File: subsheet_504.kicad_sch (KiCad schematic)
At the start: 36 parts, among them J502 Phono LEFT, J503 Phono RIGHT, U504 LF347N_mu, U508 LMC1992CCN_PHY

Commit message: pcb session 2023-01-21T22:41:51+01:00
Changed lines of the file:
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@@
     (pin "9")
   )
-  (symbol (lib_id "Device:CP1") (at 88.9 59.69 0)
+  (symbol (lib_id "Device:CP1") (at 88.9 59.69 0) (unit 1)
     (in_bom yes) (on_board yes)
     (property "Reference" "CP535" (id 0) (at 90.17 57.15 0)
@@
     (pin "2")
   )
-  (symbol (lib_id "Device:R_Small_US") (at 76.2 59.69 0)
+  (symbol (lib_id "Device:R_Small_US") (at 76.2 59.69 0) (unit 1)
     (in_bom yes) (on_board yes)
     (property "Reference" "R530" (id 0) (at 77.47 58.42 0)
@@
     (pin "2")
   )
-  (symbol (lib_id "Device:C_Small") (at 101.6 59.69 0)
+  (symbol (lib_id "Device:C_Small") (at 101.6 59.69 0) (unit 1)
     (in_bom yes) (on_board yes)
     (property "Reference" "C536" (id 0) (at 102.87 57.15 0)
@@
     (pin "2")
   )
-  (symbol (lib_id "Device:CP1") (at 38.1 26.67 270)
+  (symbol (lib_id "Device:CP1") (at 38.1 26.67 270) (unit 1)
     (in_bom yes) (on_board yes)
     (property "Reference" "CP541" (id 0) (at 35.56 22.86 90)
@@
     (pin "2")
   )
-  (symbol (lib_id "Device:CP1") (at 38.1 39.37 270)
+  (symbol (lib_id "Device:CP1") (at 38.1 39.37 270) (unit 1)
     (in_bom yes) (on_board yes)
     (property "Reference" "CP546" (id 0) (at 35.56 35.56 90)
@@
     (pin "2")
   )
-  (symbol (lib_id "Device:CP1") (at 35.56 96.52 270)
+  (symbol (lib_id "Device:CP1") (at 35.56 96.52 270) (unit 1)
     (in_bom yes) (on_board yes)
     (property "Reference" "CP544" (id 0) (at 26.67 95.25 90)
@@
     (pin "2")
   )
-  (symbol (lib_id "Device:CP1") (at 172.72 93.98 90)
+  (symbol (lib_id "Device:CP1") (at 172.72 93.98 90) (unit 1)
     (in_bom yes) (on_board yes)
     (property "Reference" "CP547" (id 0) (at 170.18 92.71 90)
@@
     (pin "2")
   )
-  (symbol (lib_id "Device:R_Small_US") (at 88.9 25.4 0)
+  (symbol (lib_id "Device:R_Small_US") (at 88.9 25.4 0) (unit 1)
     (in_bom yes) (on_board yes)
     (property "Reference" "R525" (id 0) (at 90.17 24.13 0)
@@
     (pin "2")
   )
-  (symbol (lib_id "Device:R_Small_US") (at 78.74 33.02 90)
+  (symbol (lib_id "Device:R_Small_US") (at 78.74 33.02 90) (unit 1)
     (in_bom yes) (on_board yes)
     (property "Reference" "R531" (id 0) (at 81.28 30.48 90)
@@
     (pin "2")
   )
-  (symbol (lib_id "Device:R_Small_US") (at 97.79 41.91 180)
+  (symbol (lib_id "Device:R_Small_US") (at 97.79 41.91 180) (unit 1)
     (in_bom yes) (on_board yes)
     (property "Reference" "R539" (id 0) (at 104.14 40.64 0)
@@
     (pin "2")
   )
-  (symbol (lib_id "Device:C") (at 50.8 101.6 90)
+  (symbol (lib_id "Device:C") (at 50.8 101.6 90) (unit 1)
     (in_bom yes) (on_board yes)
     (property "Reference" "C528" (id 0) (at 49.53 102.87 90)
@@
     (pin "2")
   )
-  (symbol (lib_id "Device:C") (at 20.32 127 180)
+  (symbol (lib_id "Device:C") (at 20.32 127 180) (unit 1)
     (in_bom yes) (on_board yes)
     (property "Reference" "C531" (id 0) (at 27.94 125.73 0)
@@
     (pin "2")
   )
-  (symbol (lib_id "Device:C") (at 189.23 127 180)
+  (symbol (lib_id "Device:C") (at 189.23 127 180) (unit 1)
     (in_bom yes) (on_board yes)
     (property "Reference" "C534" (id 0) (at 185.42 125.73 0)
@@
     (pin "2")
   )
-  (symbol (lib_id "Device:C") (at 158.75 99.06 270)
+  (symbol (lib_id "Device:C") (at 158.75 99.06 270) (unit 1)
     (in_bom yes) (on_board yes)
     (property "Reference" "C538" (id 0) (at 160.02 100.33 90)
@@
     (pin "2")
   )
-  (symbol (lib_id "Device:C") (at 20.32 76.2 0)
+  (symbol (lib_id "Device:C") (at 20.32 76.2 0) (unit 1)
     (in_bom yes) (on_board yes)
     (property "Reference" "C524" (id 0) (at 20.955 73.66 0)
@@
     (pin "2")
   )
-  (symbol (lib_id "Device:R_Small_US") (at 44.45 139.7 180)
+  (symbol (lib_id "Device:R_Small_US") (at 44.45 139.7 180) (unit 1)
     (in_bom yes) (on_board yes)
     (property "Reference" "R520" (id 0) (at 40.64 138.43 0))
@@
     (pin "2")
   )
-  (symbol (lib_id "Device:CP1") (at 44.45 152.4 0)
+  (symbol (lib_id "Device:CP1") (at 44.45 152.4 0) (unit 1)
     (in_bom yes) (on_board yes)
     (property "Reference" "CP525" (id 0) (at 35.56 151.13 0)
@@
     (pin "2")
   )
-  (symbol (lib_id "Device:R_Small_US") (at 38.1 190.5 270)
+  (symbol (lib_id "Device:R_Small_US") (at 38.1 190.5 270) (unit 1)
     (in_bom yes) (on_board yes)
     (property "Reference" "R590" (id 0) (at 35.56 187.96 90)
@@
     (pin "2")
   )
-  (symbol (lib_id "Device:R_Small_US") (at 165.1 139.7 180)
+  (symbol (lib_id "Device:R_Small_US") (at 165.1 139.7 180) (unit 1)
     (in_bom yes) (on_board yes)
     (property "Reference" "R533" (id 0) (at 168.91 138.43 0))
@@
     (pin "2")
   )
-  (symbol (lib_id "Device:CP1") (at 165.1 152.4 0)
+  (symbol (lib_id "Device:CP1") (at 165.1 152.4 0) (unit 1)
     (in_bom yes) (on_board yes)
     (property "Reference" "CP537" (id 0) (at 167.64 151.13 0)
@@
     (pin "2")
   )
-  (symbol (lib_id "Device:R_Small_US") (at 158.75 190.5 270)
+  (symbol (lib_id "Device:R_Small_US") (at 158.75 190.5 270) (unit 1)
     (in_bom yes) (on_board yes)
     (property "Reference" "R591" (id 0) (at 156.21 187.96 90)
@@
     (pin "2")
   )
-  (symbol (lib_id "Device:CP1") (at 57.15 133.35 0)
+  (symbol (lib_id "Device:CP1") (at 57.15 133.35 0) (unit 1)
     (in_bom yes) (on_board yes)
     (property "Reference" "CP529" (id 0) (at 59.69 132.08 0)
@@
     (pin "2")
   )
-  (symbol (lib_id "Device:R_Small_US") (at 57.15 146.05 180)
+  (symbol (lib_id "Device:R_Small_US") (at 57.15 146.05 180) (unit 1)
     (in_bom yes) (on_board yes)
     (property "Reference" "R527" (id 0) (at 60.96 144.78 0))
@@
     (pin "2")
   )
-  (symbol (lib_id "Device:R_Small_US") (at 73.66 153.67 270)
+  (symbol (lib_id "Device:R_Small_US") (at 73.66 153.67 270) (unit 1)
     (in_bom yes) (on_board yes)
     (property "Reference" "R524" (id 0) (at 66.04 152.4 90)
@@
     (pin "2")
   )
-  (symbol (lib_id "Device:R_Small_US") (at 90.17 171.45 180)
+  (symbol (lib_id "Device:R_Small_US") (at 90.17 171.45 180) (unit 1)
     (in_bom yes) (on_board yes)
     (property "Reference" "R540" (id 0) (at 93.98 170.18 0))
@@
     (pin "2")
   )
-  (symbol (lib_id "Device:CP1") (at 152.4 133.35 0)
+  (symbol (lib_id "Device:CP1") (at 152.4 133.35 0) (unit 1)
     (in_bom yes) (on_board yes)
     (property "Reference" "CP543" (id 0) (at 154.94 132.08 0)
@@
     (pin "2")
   )
-  (symbol (lib_id "Device:R_Small_US") (at 152.4 146.05 180)
+  (symbol (lib_id "Device:R_Small_US") (at 152.4 146.05 180) (unit 1)
     (in_bom yes) (on_board yes)
     (property "Reference" "R538" (id 0) (at 156.21 144.78 0))
@@
     (pin "2")
   )
-  (symbol (lib_id "Device:R_Small_US") (at 135.89 153.67 90)
+  (symbol (lib_id "Device:R_Small_US") (at 135.89 153.67 90) (unit 1)
     (in_bom yes) (on_board yes)
     (property "Reference" "R537" (id 0) (at 133.35 152.4 90)
@@
     (pin "2")
   )
-  (symbol (lib_id "Device:R_Small_US") (at 119.38 171.45 180)
+  (symbol (lib_id "Device:R_Small_US") (at 119.38 171.45 180) (unit 1)
     (in_bom yes) (on_board yes)
     (property "Reference" "R541" (id 0) (at 123.19 170.18 0))
@@
     (pin "2")
   )
-  (symbol (lib_id "lf347:LF347N_mu") (at 73.66 166.37 0) (mirror x)
+  (symbol (lib_id "lf347:LF347N_mu") (at 73.66 166.37 0) (mirror x) (unit 1)
     (in_bom yes) (on_board yes)
     (property "Reference" "U504" (id 0) (at 67.31 171.45 0)
@@
       (effects (font (size 1.27 1.27)) (justify left top) hide)
     )
-    (pin "5")
-    (pin "6")
-    (pin "7")
-  )
-  (symbol (lib_id "lf347:LF347N_mu") (at 135.89 158.75 0) (mirror y)
+    (pin "1")
+    (pin "2")
+    (pin "3")
+  )
+  (symbol (lib_id "lf347:LF347N_mu") (at 135.89 158.75 0) (mirror y) (unit 1)
     (in_bom yes) (on_board yes)
     (property "Reference" "U504" (id 0) (at 135.89 167.64 0)
@@
       (effects (font (size 1.27 1.27)) (justify left top) hide)
     )
-    (pin "10")
-    (pin "8")
-    (pin "9")
-  )
-  (symbol (lib_id "Device:CP1") (at 154.94 81.28 90)
+    (pin "1")
+    (pin "2")
+    (pin "3")
+  )
+  (symbol (lib_id "Device:CP1") (at 154.94 81.28 90) (unit 1)
     (in_bom yes) (on_board yes)
     (property "Reference" "CP542" (id 0) (at 163.83 80.01 90)
@@
     (pin "2")
   )
-  (symbol (lib_id "Device:R_Small_US") (at 88.9 41.91 0)
+  (symbol (lib_id "Device:R_Small_US") (at 88.9 41.91 0) (unit 1)
     (in_bom yes) (on_board yes)
     (property "Reference" "R2701" (id 0) (at 90.17 40.64 0)

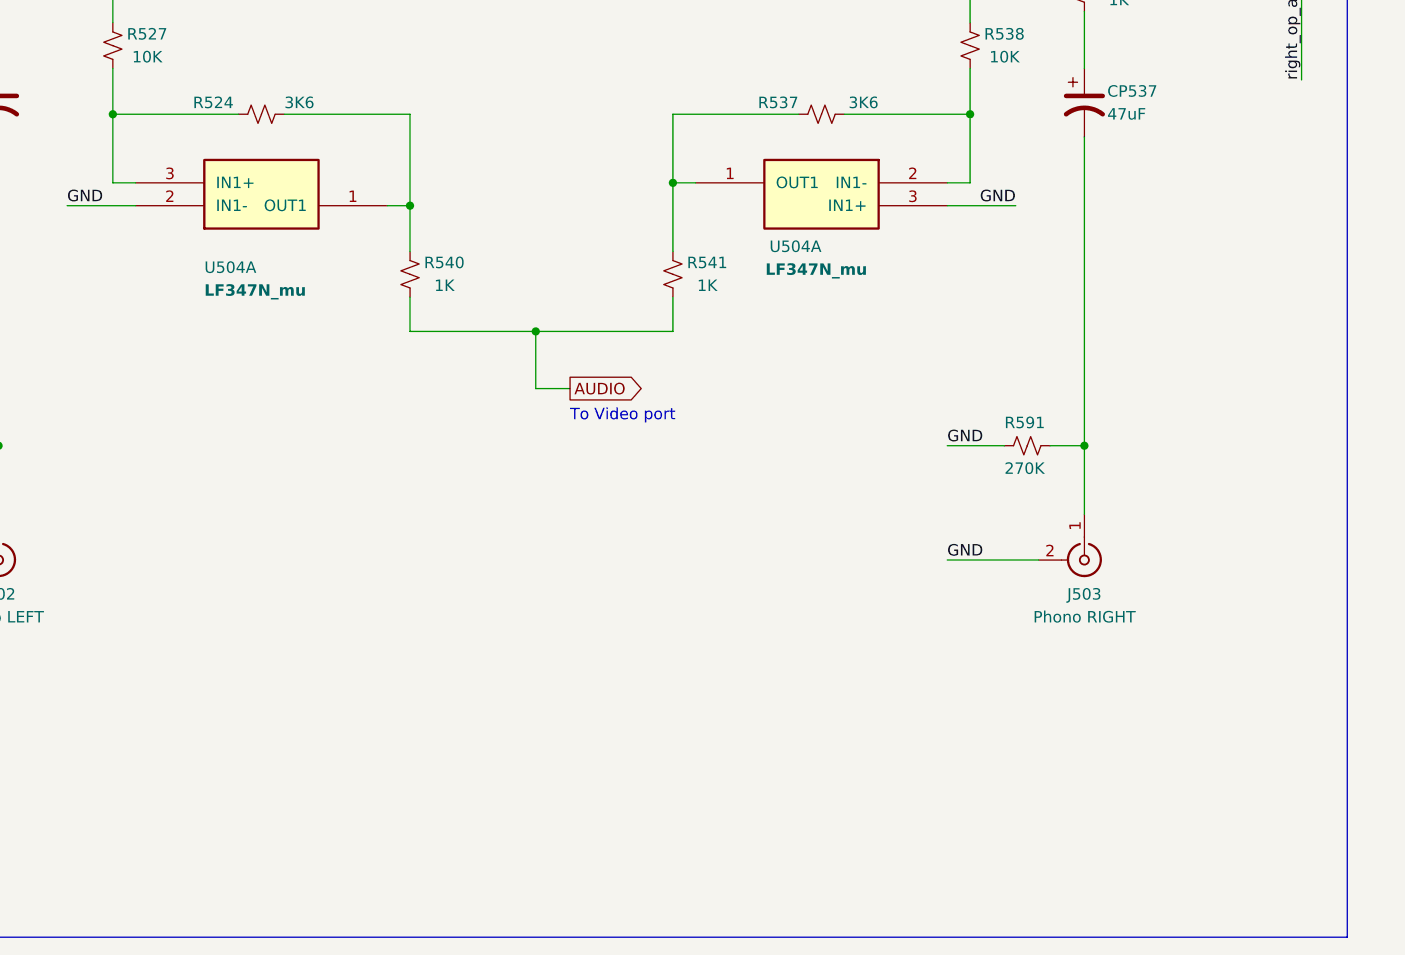
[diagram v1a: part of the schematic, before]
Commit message: add gnd/vcc symbol to start replacing local labels
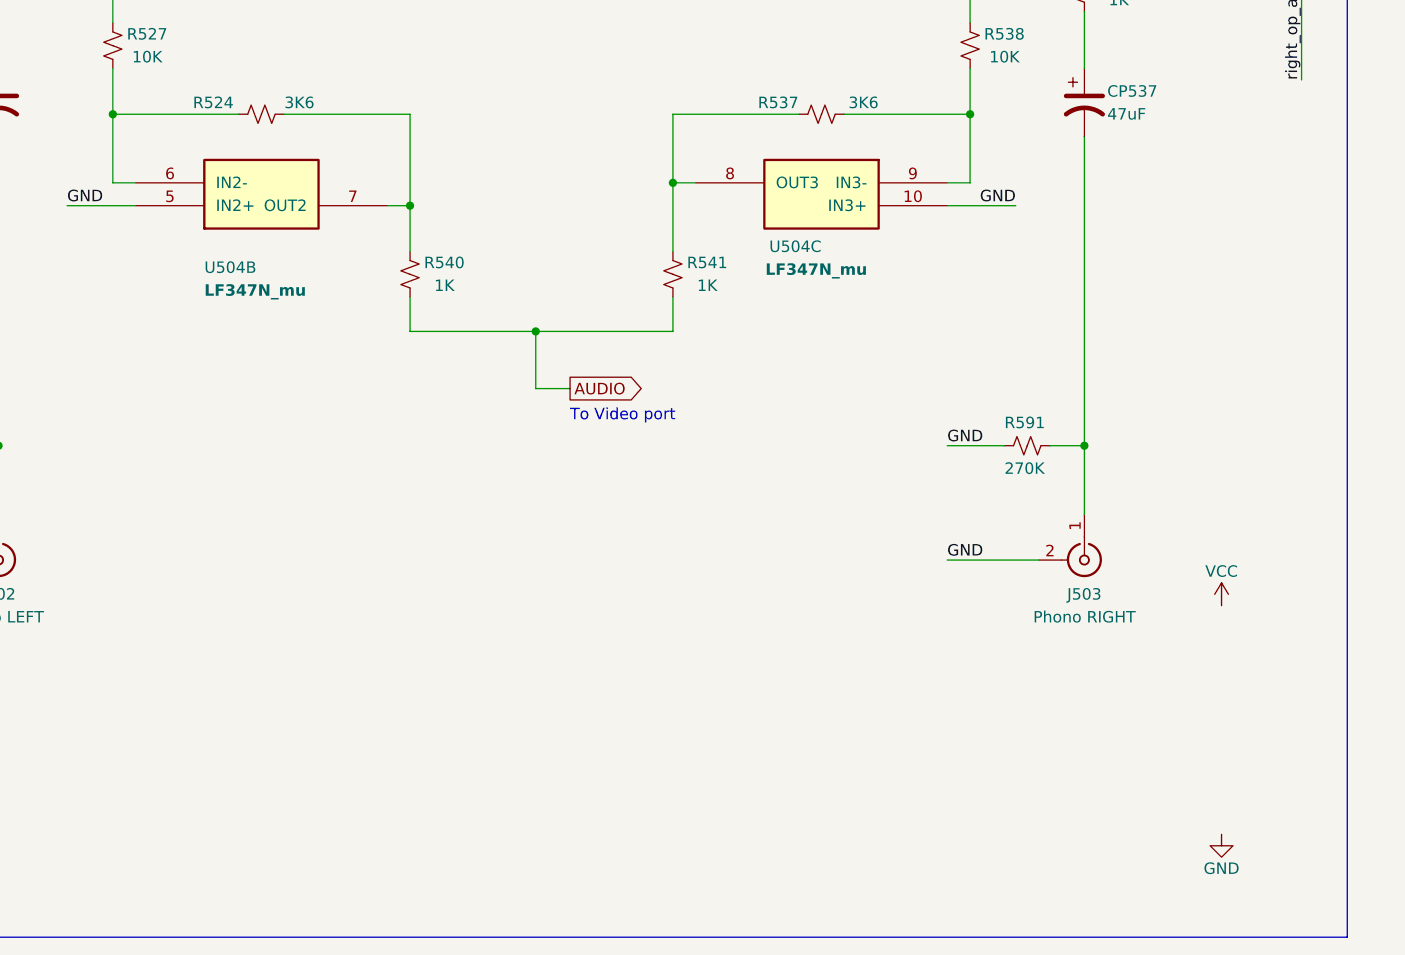
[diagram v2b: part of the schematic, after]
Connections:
- net GND: now also U504.10 (IN3+), U504.5 (IN2+); no longer U504.2 (IN1-), U504.3 (IN1+)
- net at R524.2, R527.1: now also U504.6 (IN2-); no longer U504.3 (IN1+)
- net at R524.1, R540.2: now also U504.7 (OUT2); no longer U504.1 (OUT1)
- net at R537.2, R538.1: now also U504.9 (IN3-); no longer U504.2 (IN1-)
- net at R537.1, R541.2: now also U504.8 (OUT3); no longer U504.1 (OUT1)
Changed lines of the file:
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@@
     (pin "2")
   )
-  (symbol (lib_id "lf347:LF347N_mu") (at 73.66 166.37 0) (mirror x) (unit 1)
+  (symbol (lib_id "lf347:LF347N_mu") (at 73.66 166.37 0) (mirror x) (unit 2)
     (in_bom yes) (on_board yes)
     (property "Reference" "U504" (id 0) (at 67.31 171.45 0)
@@
       (effects (font (size 1.27 1.27)) (justify left top) hide)
     )
-    (pin "1")
-    (pin "2")
-    (pin "3")
+    (pin "5")
+    (pin "6")
+    (pin "7")
   )
-  (symbol (lib_id "lf347:LF347N_mu") (at 135.89 158.75 0) (mirror y) (unit 1)
+  (symbol (lib_id "lf347:LF347N_mu") (at 135.89 158.75 0) (mirror y) (unit 3)
     (in_bom yes) (on_board yes)
     (property "Reference" "U504" (id 0) (at 135.89 167.64 0)
@@
       (effects (font (size 1.27 1.27)) (justify left top) hide)
     )
-    (pin "1")
-    (pin "2")
-    (pin "3")
+    (pin "10")
+    (pin "8")
+    (pin "9")
   )
   (symbol (lib_id "Device:CP1") (at 154.94 81.28 90) (unit 1)
@@
     (pin "2")
   )
+  (symbol (lib_id "power:VCC") (at 180.34 208.28 0) (unit 1)
+    (in_bom yes) (on_board yes)
+    (property "Reference" "#PWR?" (id 0) (at 180.34 212.09 0)
+      (effects (font (size 1.27 1.27)) hide)
+    )
+    (property "Value" "VCC" (id 1) (at 180.34 204.47 0))
+    (property "Footprint" "" (id 2) (at 180.34 208.28 0)
+      (effects (font (size 1.27 1.27)) hide)
+    )
+    (property "Datasheet" "" (id 3) (at 180.34 208.28 0)
+      (effects (font (size 1.27 1.27)) hide)
+    )
+    (pin "1")
+  )
+  (symbol (lib_id "power:GND") (at 180.34 233.68 0) (unit 1)
+    (in_bom yes) (on_board yes)
+    (property "Reference" "#PWR?" (id 0) (at 180.34 240.03 0)
+      (effects (font (size 1.27 1.27)) hide)
+    )
+    (property "Value" "GND" (id 1) (at 180.34 237.49 0))
+    (property "Footprint" "" (id 2) (at 180.34 233.68 0)
+      (effects (font (size 1.27 1.27)) hide)
+    )
+    (property "Datasheet" "" (id 3) (at 180.34 233.68 0)
+      (effects (font (size 1.27 1.27)) hide)
+    )
+    (pin "1")
+  )
 )
